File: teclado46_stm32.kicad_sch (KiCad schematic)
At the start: 15 parts, among them J1 78171-0004, U1 XC6206PxxxMR, U2 STM32G0B1CBTx

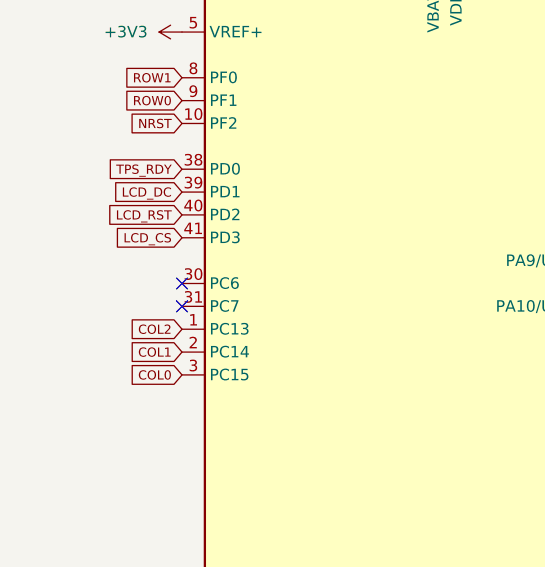
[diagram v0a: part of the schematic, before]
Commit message: chore: routed open-drain
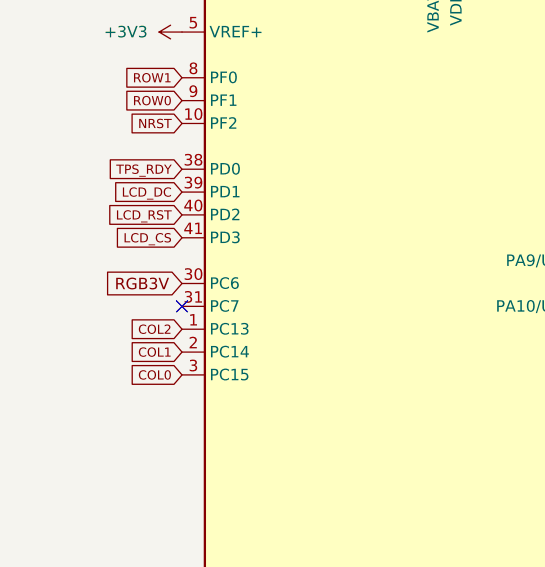
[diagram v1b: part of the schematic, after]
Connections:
- net RGB3V: now also U2.30 (PC6)
- no-connect marks 18 -> 17
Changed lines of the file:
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@@
-	)
-	(no_connect
-		(at 31.75 90.17)
 	)
 	(no_connect
@@
 				)
 				(justify right)
+				(hide yes)
+			)
+		)
+	)
+	(global_label "RGB3V"
+		(shape input)
+		(at 31.75 90.17 180)
+		(fields_autoplaced yes)
+		(effects
+			(font
+				(size 1.27 1.27)
+			)
+			(justify right)
+		)
+		(property "Intersheetrefs" "${INTERSHEET_REFS}"
+			(at 22.6567 90.17 0)
+			(effects
+				(font
+					(size 1.27 1.27)
+				)
+				(justify right)

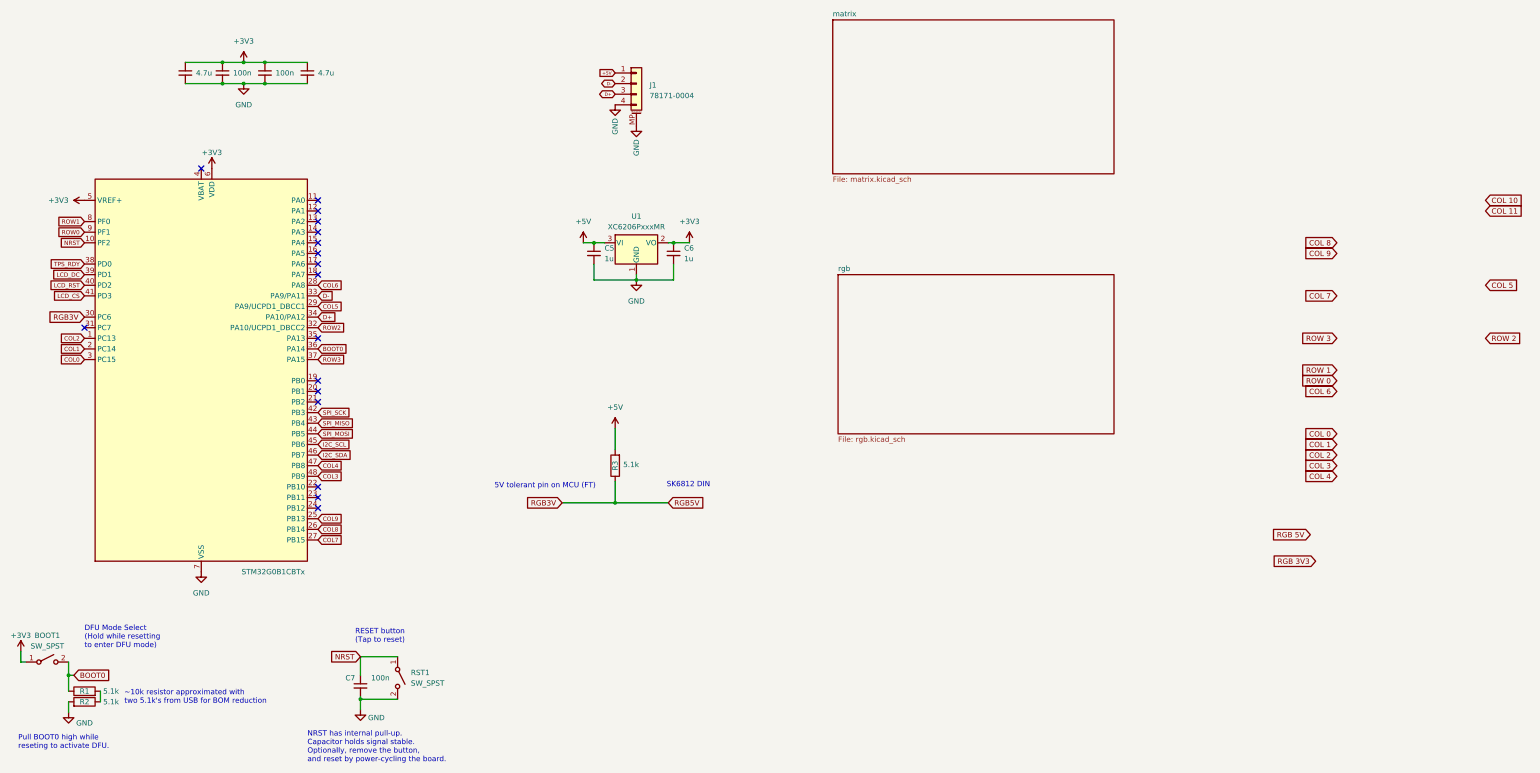
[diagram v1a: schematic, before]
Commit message: chore: routed rows and columns
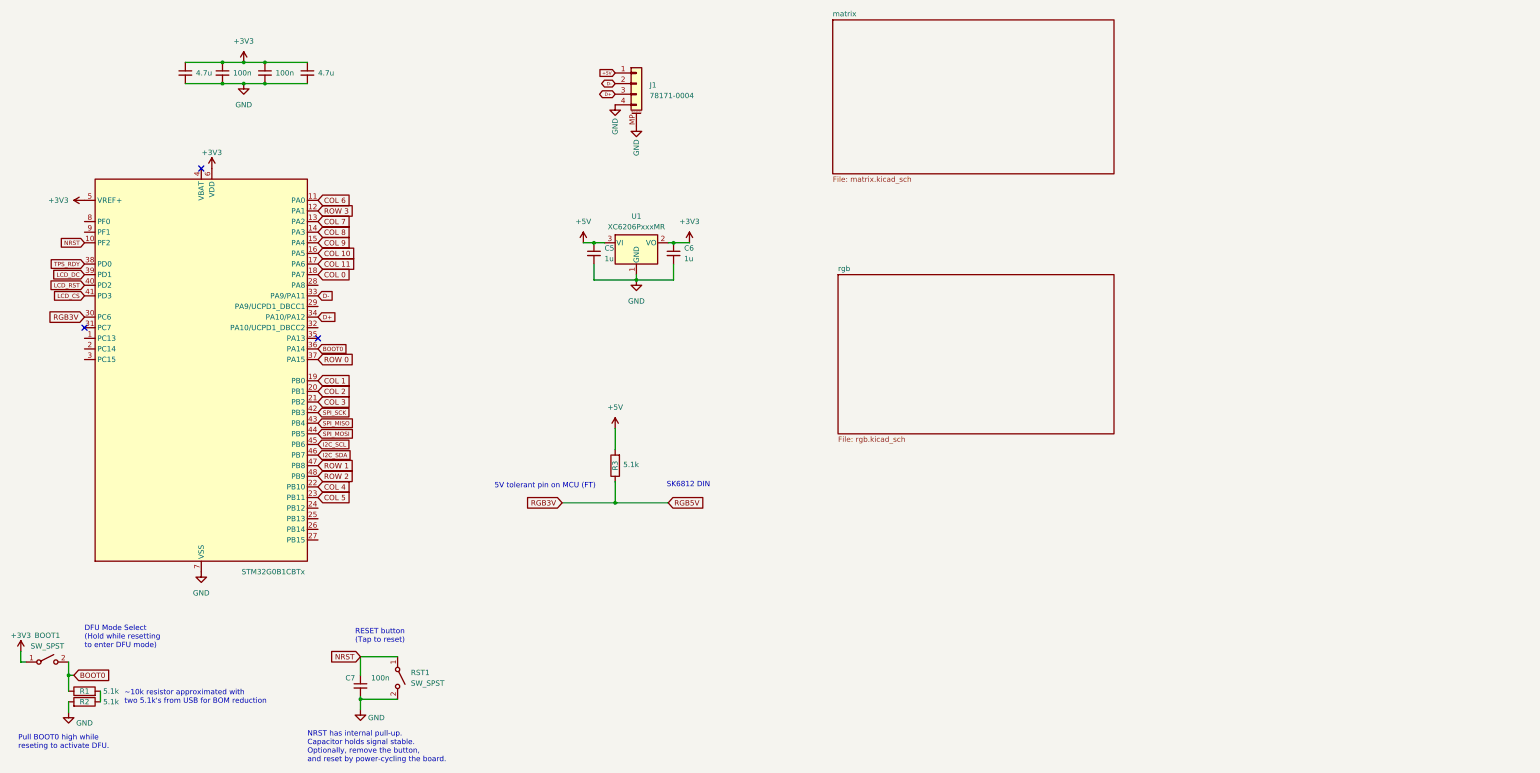
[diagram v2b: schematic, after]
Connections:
- net COL3 is gone; now on net ROW 2: U2.48 (PB9)
- net COL4 is gone; now on net ROW 1: U2.47 (PB8)
- net ROW3 is gone; now on net ROW 0: U2.37 (PA15)
- net COL 0: now also U2.18 (PA7)
- net COL 1: now also U2.19 (PB0)
- net COL 10: now also U2.16 (PA5)
- net COL 11: now also U2.17 (PA6)
- net COL 2: now also U2.20 (PB1)
- net COL 3: now also U2.21 (PB2)
- net COL 4: now also U2.22 (PB10)
- net COL 5: now also U2.23 (PB11)
- net COL 6: now also U2.11 (PA0)
- net COL 7: now also U2.13 (PA2)
- net COL 8: now also U2.14 (PA3)
- net COL 9: now also U2.15 (PA4)
- net ROW 3: now also U2.12 (PA1)
- net COL0: no longer names the net of U2.3 (PC15)
- net COL1: no longer names the net of U2.2 (PC14)
- net COL2: no longer names the net of U2.1 (PC13)
- net COL5: no longer names the net of U2.29 (PA9/UCPD1_DBCC1)
- net COL6: no longer names the net of U2.28 (PA8)
- net COL7: no longer names the net of U2.27 (PB15)
- net COL8: no longer names the net of U2.26 (PB14)
- net COL9: no longer names the net of U2.25 (PB13)
- net ROW0: no longer names the net of U2.9 (PF1)
- net ROW1: no longer names the net of U2.8 (PF0)
- net ROW2: no longer names the net of U2.32 (PA10/UCPD1_DBCC2)
- no-connect marks 17 -> 3

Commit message: chore: changed cap footprint
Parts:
- C1, C3, C4: footprint Capacitor_SMD:C_0805_2012Metric -> Capacitor_SMD:C_0402_1005Metric
- C2: footprint Capacitor_SMD:C_0805_2012Metric -> Capacitor_SMD:C_0402_1005Metric; LCSC (none) -> C1525
- C7: LCSC C307331 -> C1525
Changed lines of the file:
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@@
 			)
 		)
-		(property "Footprint" "Capacitor_SMD:C_0805_2012Metric"
+		(property "Footprint" "Capacitor_SMD:C_0402_1005Metric"
 			(at 74.93 31.75 0)
 			(effects
@@
 			)
 		)
-		(property "Footprint" "Capacitor_SMD:C_0805_2012Metric"
+		(property "Footprint" "Capacitor_SMD:C_0402_1005Metric"
 			(at 64.77 31.75 0)
 			(effects
@@
 		)
 		(property "Description" "Unpolarized capacitor, small symbol"
+			(at 64.77 31.75 0)
+			(effects
+				(font
+					(size 1.27 1.27)
+				)
+				(hide yes)
+			)
+		)
+		(property "LCSC" "C1525"
 			(at 64.77 31.75 0)
 			(effects
@@
 			)
 		)
-		(property "Footprint" "Capacitor_SMD:C_0805_2012Metric"
+		(property "Footprint" "Capacitor_SMD:C_0402_1005Metric"
 			(at 85.09 31.75 0)
 			(effects
@@
 					(size 1.27 1.27)
 				)
-			)
-		)
-		(property "LCSC" "C307331"
+				(hide yes)
+			)
+		)
+		(property "LCSC" "C1525"
 			(at 97.79 178.435 0)
 			(effects
@@
 			)
 		)
-		(property "Footprint" "Capacitor_SMD:C_0805_2012Metric"
+		(property "Footprint" "Capacitor_SMD:C_0402_1005Metric"
 			(at 55.88 31.75 0)
 			(effects

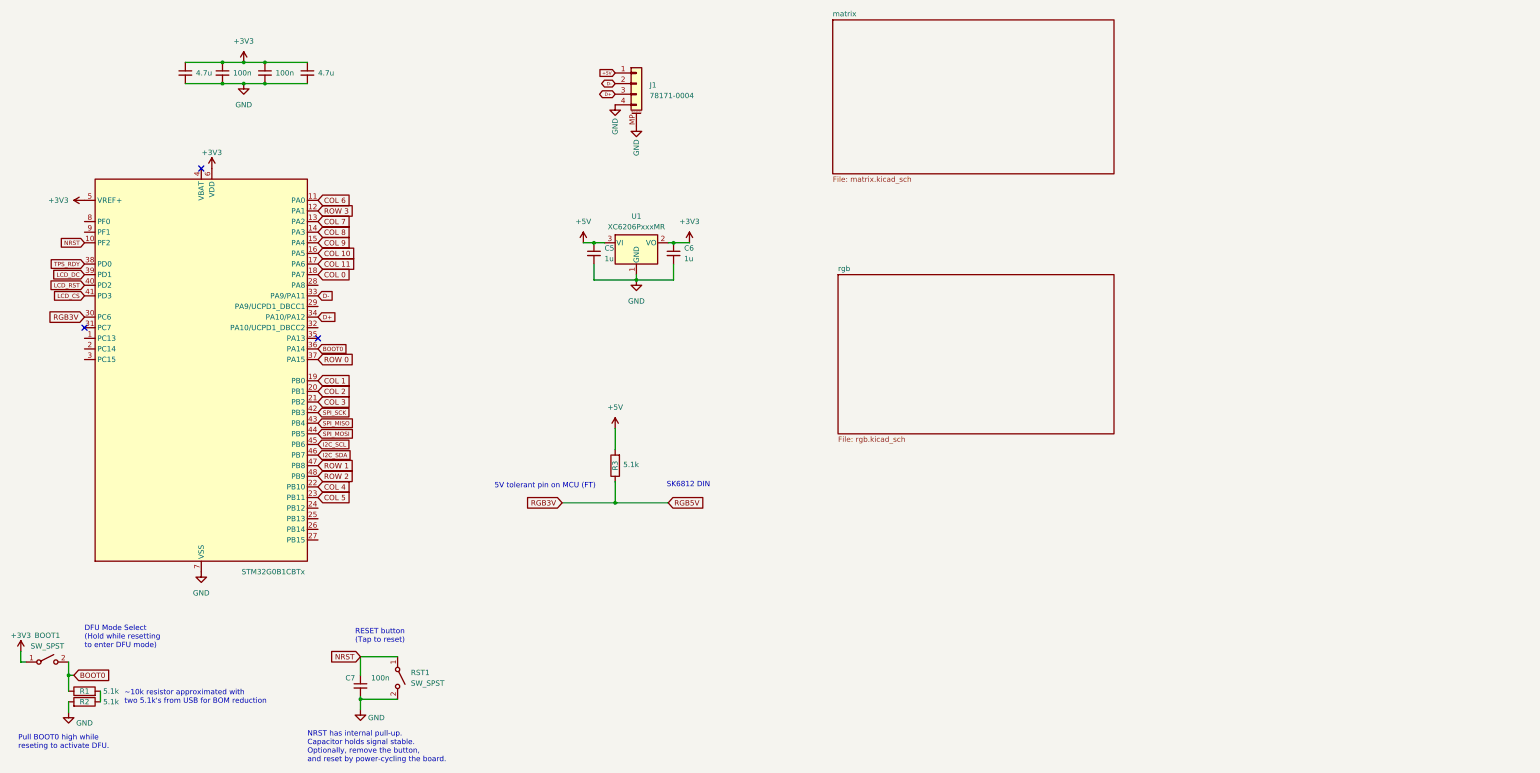
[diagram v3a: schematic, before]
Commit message: chore: added lcsc part numbers
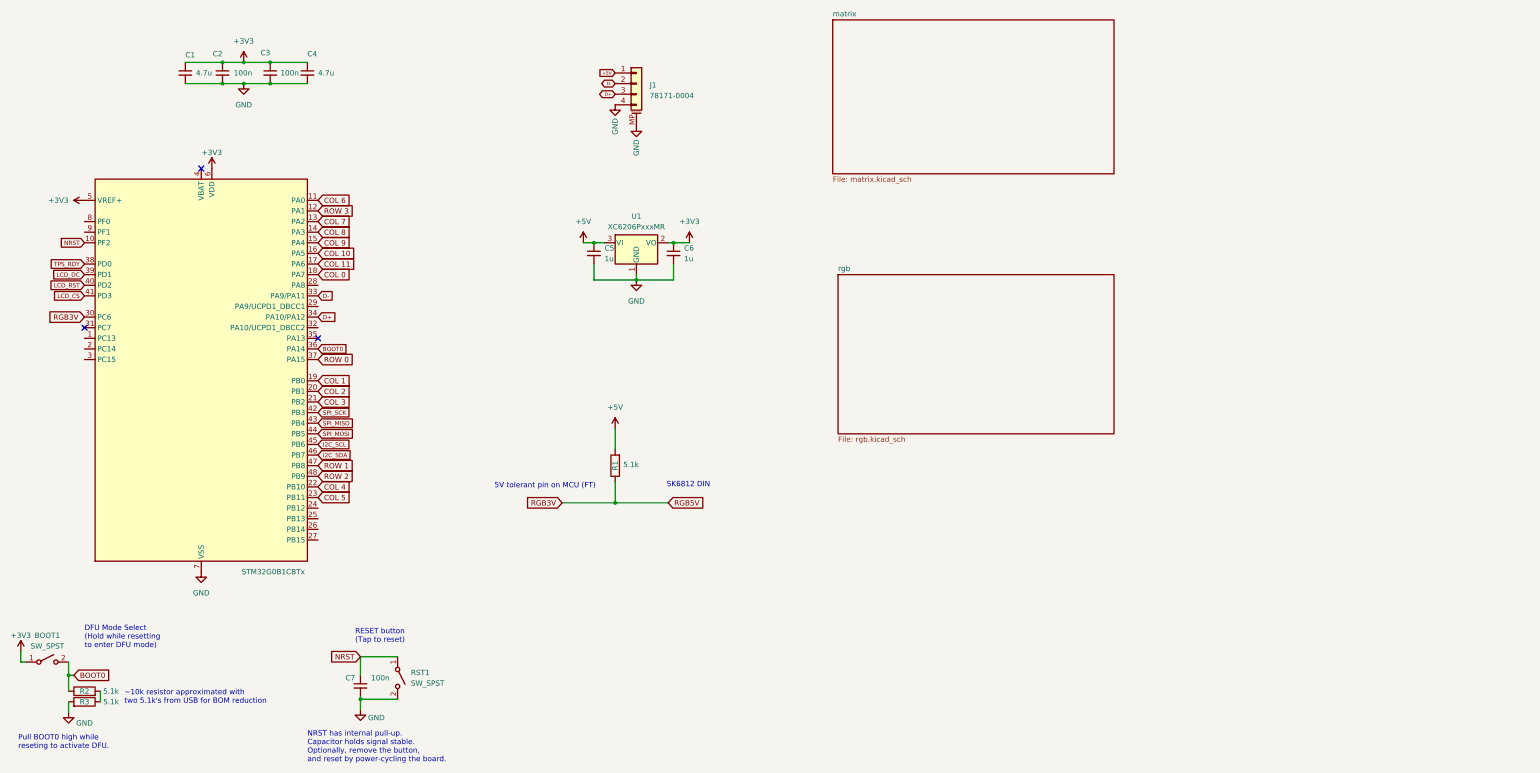
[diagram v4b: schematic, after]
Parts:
- BOOT1, RST1: LCSC (none) -> C318884
- C1, C4: LCSC (none) -> C23733
- C3: LCSC (none) -> C1525
- C5, C6: LCSC (none) -> C52923
- J1: LCSC (none) -> C588524; LCSC Part Number C588524 -> (none)
- R1: renamed from R3; LCSC (none) -> C25905
- R2: renamed from R1; LCSC (none) -> C25905
- R3: renamed from R2; LCSC (none) -> C25905
- U2: LCSC (none) -> C2847904

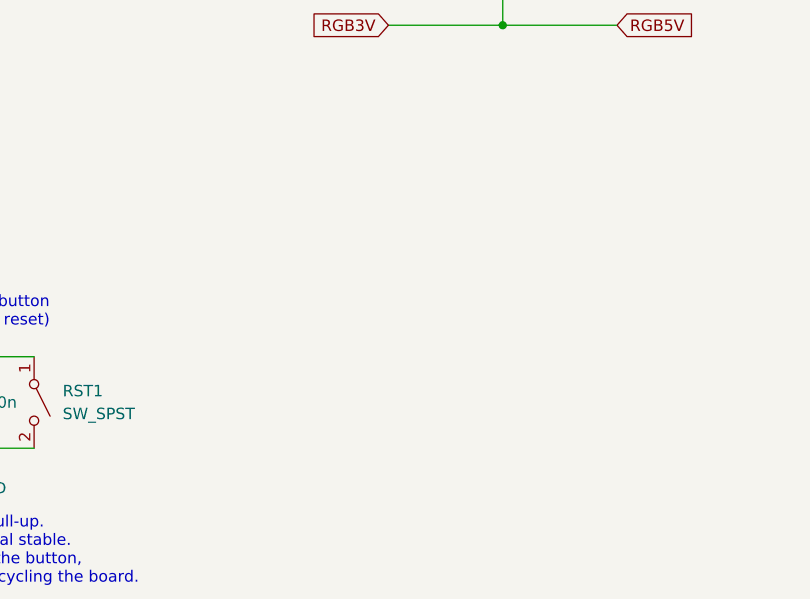
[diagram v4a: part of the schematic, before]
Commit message: chore: add mounting holes
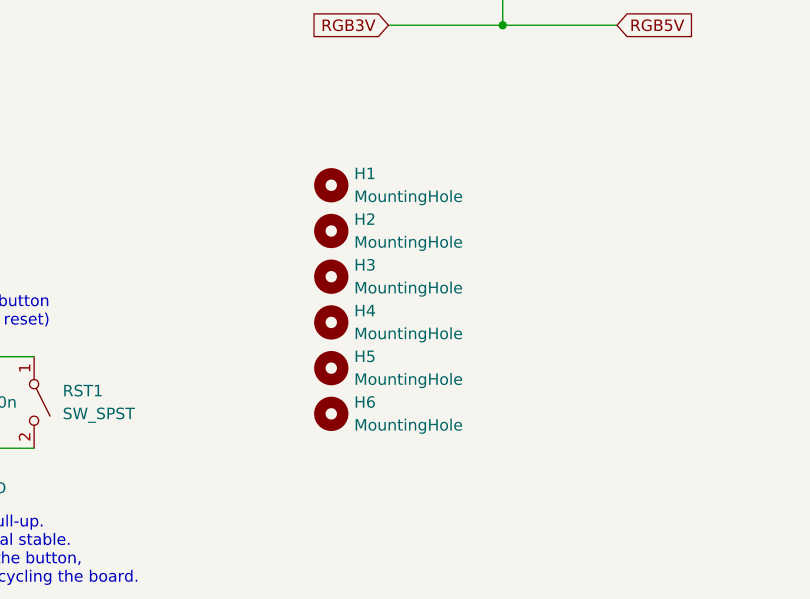
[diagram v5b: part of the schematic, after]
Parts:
- added H1, H2, H3, H4, H5, H6: MountingHole, MountingHole:MountingHole_2.2mm_M2, symbol Mechanical:MountingHole

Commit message: chore: changed mcu orientation and rerouted columns
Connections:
- net COL 1: now also U2.17 (PA6); no longer U2.19 (PB0)
- net COL 10: now also U2.20 (PB1); no longer U2.16 (PA5)
- net COL 11: now also U2.19 (PB0); no longer U2.17 (PA6)
- net COL 2: now also U2.16 (PA5); no longer U2.20 (PB1)
- net COL 3: now also U2.15 (PA4); no longer U2.21 (PB2)
- net COL 4: now also U2.14 (PA3); no longer U2.22 (PB10)
- net COL 5: now also U2.13 (PA2); no longer U2.23 (PB11)
- net COL 6: now also U2.24 (PB12); no longer U2.11 (PA0)
- net COL 7: now also U2.23 (PB11); no longer U2.13 (PA2)
- net COL 8: now also U2.22 (PB10); no longer U2.14 (PA3)
- net COL 9: now also U2.21 (PB2); no longer U2.15 (PA4)
- net ROW 0: no longer U2.37 (PA15)
- net ROW 1: no longer U2.47 (PB8)
- net ROW 2: no longer U2.48 (PB9)
- net ROW 3: no longer U2.12 (PA1)
- no-connect marks 3 -> 1

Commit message: chore: rerouted led din
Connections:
- net RGB3V: now also U2.37 (PA15); no longer U2.30 (PC6)
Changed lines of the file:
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@@
 	(global_label "RGB3V"
 		(shape input)
-		(at 31.75 90.17 180)
+		(at 87.63 100.33 0)
 		(fields_autoplaced yes)
 		(effects
@@
 				(size 1.27 1.27)
 			)
-			(justify right)
+			(justify left)
 		)
 		(property "Intersheetrefs" "${INTERSHEET_REFS}"
-			(at 22.6567 90.17 0)
+			(at 96.7233 100.33 0)
 			(effects
 				(font
 					(size 1.27 1.27)
 				)
-				(justify right)
+				(justify left)
 				(hide yes)
 			)

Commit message: chore: rerouted entire board
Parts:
- removed H5, H6: MountingHole, MountingHole:MountingHole_2.2mm_M2, symbol Mechanical:MountingHole
- BOOT1, RST1: footprint Button_Switch_SMD:SW_SPST_TL3342 -> Button_Switch_SMD:SW_SPST_TS-1088-xR020
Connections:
- net COL 0: now also U2.13 (PA2); no longer U2.18 (PA7)
- net COL 1: now also U2.14 (PA3); no longer U2.17 (PA6)
- net COL 10: now also U2.23 (PB11); no longer U2.20 (PB1)
- net COL 11: now also U2.24 (PB12); no longer U2.19 (PB0)
- net COL 2: now also U2.15 (PA4); no longer U2.16 (PA5)
- net COL 3: now also U2.17 (PA6); no longer U2.15 (PA4)
- net COL 4: now also U2.18 (PA7); no longer U2.14 (PA3)
- net COL 5: now also U2.16 (PA5); no longer U2.13 (PA2)
- net COL 6: now also U2.21 (PB2); no longer U2.24 (PB12)
- net COL 7: now also U2.19 (PB0); no longer U2.23 (PB11)
- net COL 8: now also U2.20 (PB1); no longer U2.22 (PB10)
- net COL 9: now also U2.22 (PB10); no longer U2.21 (PB2)
- net ROW 0: now also U2.25 (PB13)
- net ROW 1: now also U2.26 (PB14)
- net ROW 2: now also U2.27 (PB15)
- net ROW 3: now also U2.1 (PC13)
